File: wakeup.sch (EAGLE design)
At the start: 14 parts, among them IC2 ATMEGA48/88/168-AU

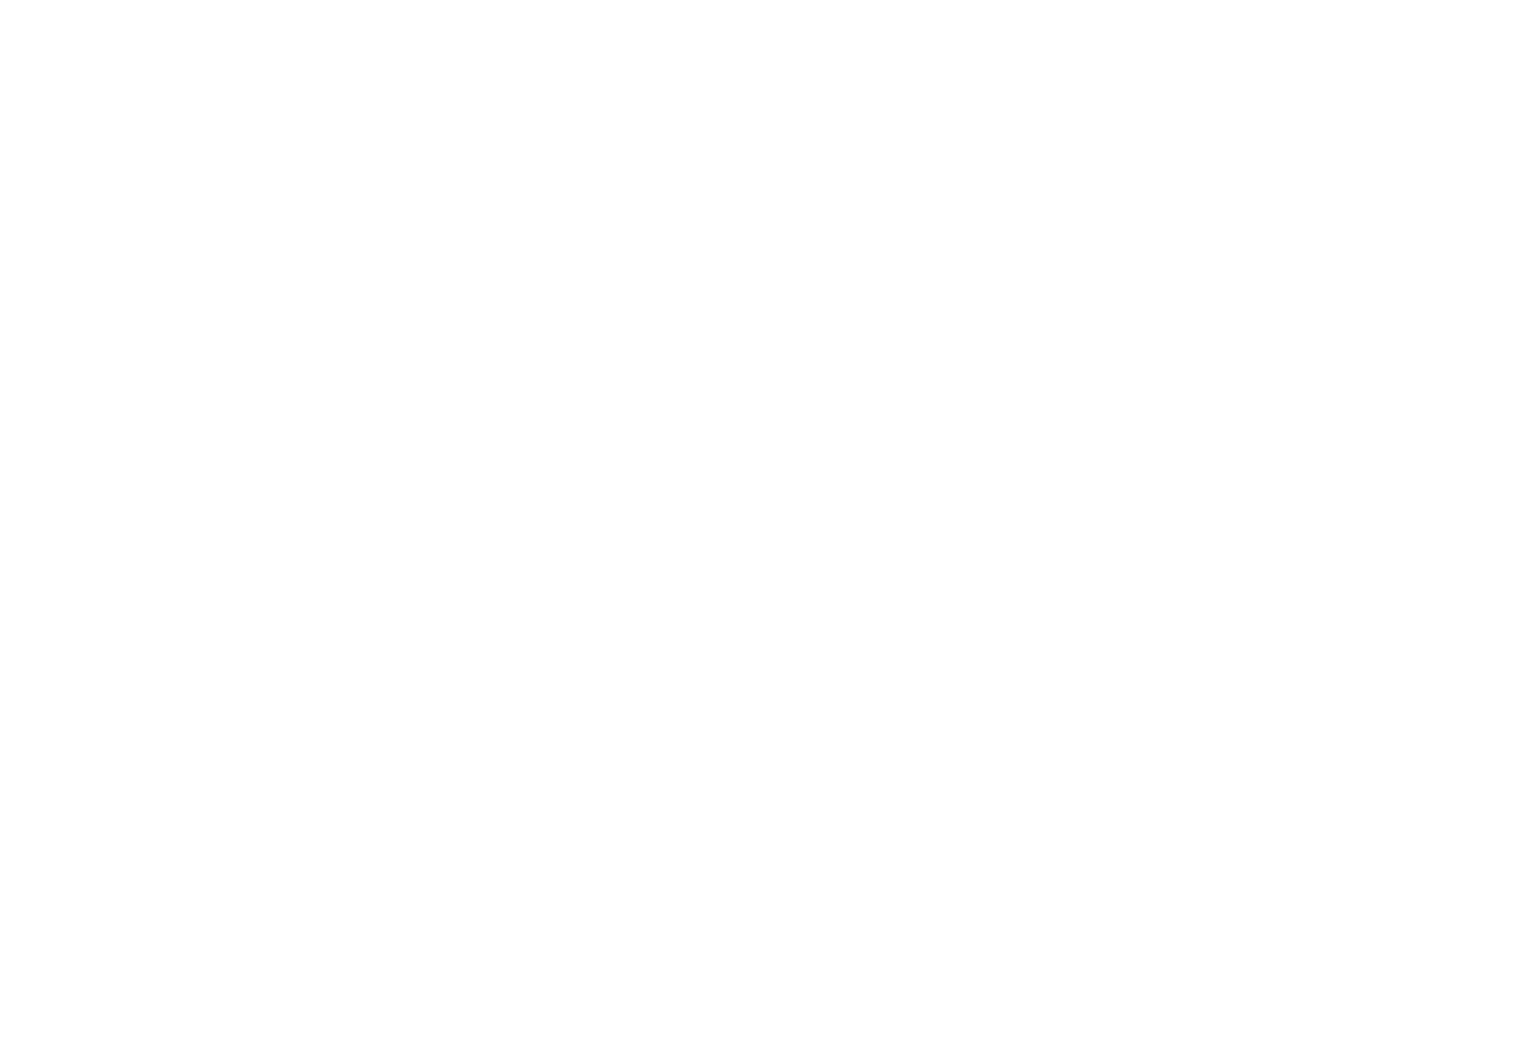
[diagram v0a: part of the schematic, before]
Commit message: Added RaspberryPi Library
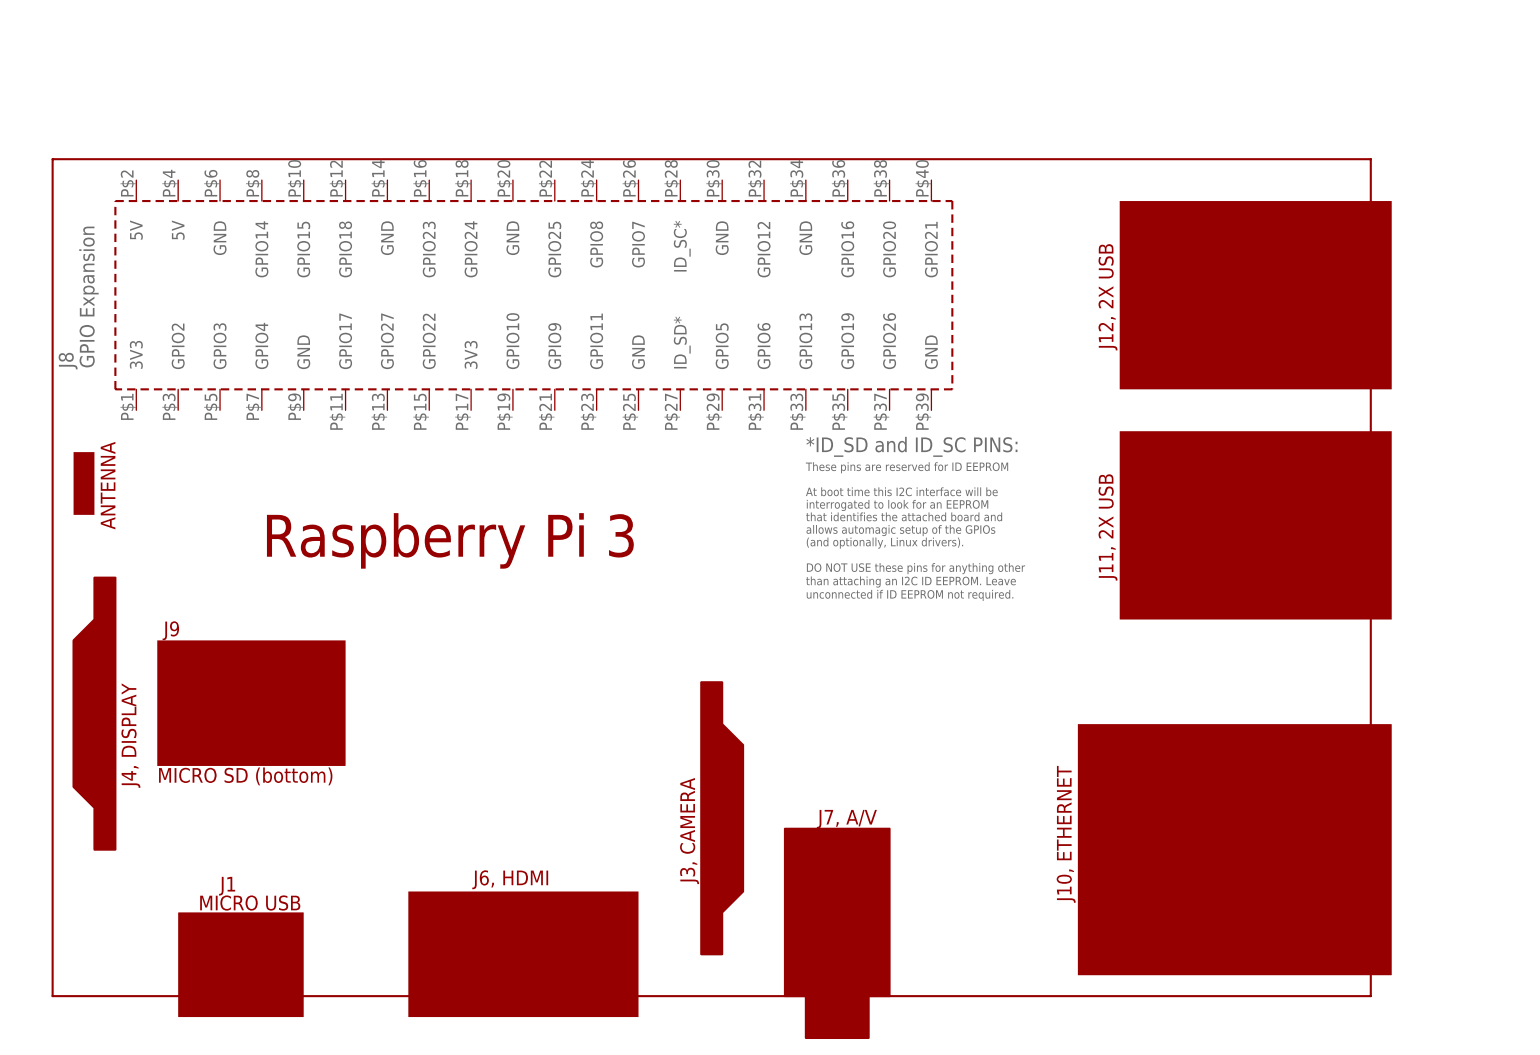
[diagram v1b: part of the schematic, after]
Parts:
- added PCB1: RPI3, e14_Rpi3_RevA:RPI3
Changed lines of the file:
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@@
 <?xml version="1.0" encoding="utf-8"?>
 <!DOCTYPE eagle SYSTEM "eagle.dtd">
-<eagle version="6.2">
+<eagle version="7.7.0">
 <drawing>
 <settings>
@@
 <layers>
 <layer number="1" name="Top" color="4" fill="1" visible="no" active="no"/>
+<layer number="2" name="Route2" color="1" fill="3" visible="no" active="no"/>
+<layer number="3" name="Route3" color="4" fill="3" visible="no" active="no"/>
+<layer number="4" name="Route4" color="1" fill="4" visible="no" active="no"/>
+<layer number="5" name="Route5" color="4" fill="4" visible="no" active="no"/>
+<layer number="6" name="Route6" color="1" fill="8" visible="no" active="no"/>
+<layer number="7" name="Route7" color="4" fill="8" visible="no" active="no"/>
+<layer number="8" name="Route8" color="1" fill="2" visible="no" active="no"/>
+<layer number="9" name="Route9" color="4" fill="2" visible="no" active="no"/>
+<layer number="10" name="Route10" color="1" fill="7" visible="no" active="no"/>
+<layer number="11" name="Route11" color="4" fill="7" visible="no" active="no"/>
+<layer number="12" name="Route12" color="1" fill="5" visible="no" active="no"/>
+<layer number="13" name="Route13" color="4" fill="5" visible="no" active="no"/>
+<layer number="14" name="Route14" color="1" fill="6" visible="no" active="no"/>
+<layer number="15" name="Route15" color="4" fill="6" visible="no" active="no"/>
 <layer number="16" name="Bottom" color="1" fill="1" visible="no" active="no"/>
 <layer number="17" name="Pads" color="2" fill="1" visible="no" active="no"/>
@@
 <layer number="51" name="tDocu" color="7" fill="1" visible="no" active="no"/>
 <layer number="52" name="bDocu" color="7" fill="1" visible="no" active="no"/>
+<layer number="90" name="Modules" color="5" fill="1" visible="yes" active="yes"/>
 <layer number="91" name="Nets" color="2" fill="1" visible="yes" active="yes"/>
 <layer number="92" name="Busses" color="1" fill="1" visible="yes" active="yes"/>
@@
 <part name="P+4" library="supply1" deviceset="VCC" device=""/>
 <part name="GND12" library="supply1" deviceset="GND" device=""/>
+<part name="PCB1" library="e14_Rpi3_RevA" deviceset="RPI3" device=""/>
 </parts>
 <sheets>
@@
 <instance part="P+4" gate="VCC" x="-27.94" y="45.72"/>
 <instance part="GND12" gate="1" x="-27.94" y="-2.54"/>
+<instance part="PCB1" gate="G$1" x="-96.52" y="-193.04"/>
 </instances>
 <busses>
@@
 </schematic>
 </drawing>
+<compatibility>
+<note version="6.3" minversion="6.2.2" severity="warning">
+Since Version 6.2.2 text objects can contain more than one line,
+which will not be processed correctly with this version.
+</note>
+</compatibility>
 </eagle>

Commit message: Updated board and schematics for RaspberryPI
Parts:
- removed PCB1: RPI3, e14_Rpi3_RevA:RPI3
- added C1: 100nF, resistor:C-EUC0805K
- added CFG: (no value), FLYFISH:PIN2_100
- added K1: PIN20X2, FLYFISH:PIN20X2
- added R1, R2: 3k9, resistor:R-EU_M0805
- added R3: 1k, resistor:R-EU_M0805
- added U1: EEPROM24, FLYFISH:EEPROM24
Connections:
- new net +3V3: C1.1, K1.1, K1.17, R1.2, R2.2, R3.2, U1.VCC
- new net +5V: K1.2, K1.4
- new net N$1: K1.28, R1.1, U1.SCL
- new net N$2: K1.27, R2.1, U1.SDA
- new net N$3: CFG.1, R3.1, U1.WP
- net GND: now also C1.2, CFG.2, K1.14, K1.20, K1.25, K1.30, K1.34, K1.39, K1.6, K1.9, U1.A0, U1.A1, U1.A2, U1.GND
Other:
- note added: "Checked by:"
- note added: "Drawn by:"
- note added: "v0.1"
- moved on the sheet: C2, C3, IC2, SL1, SL2-1, SL2-2, SV1, U$1, U$2, U$3, U$4, U$5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

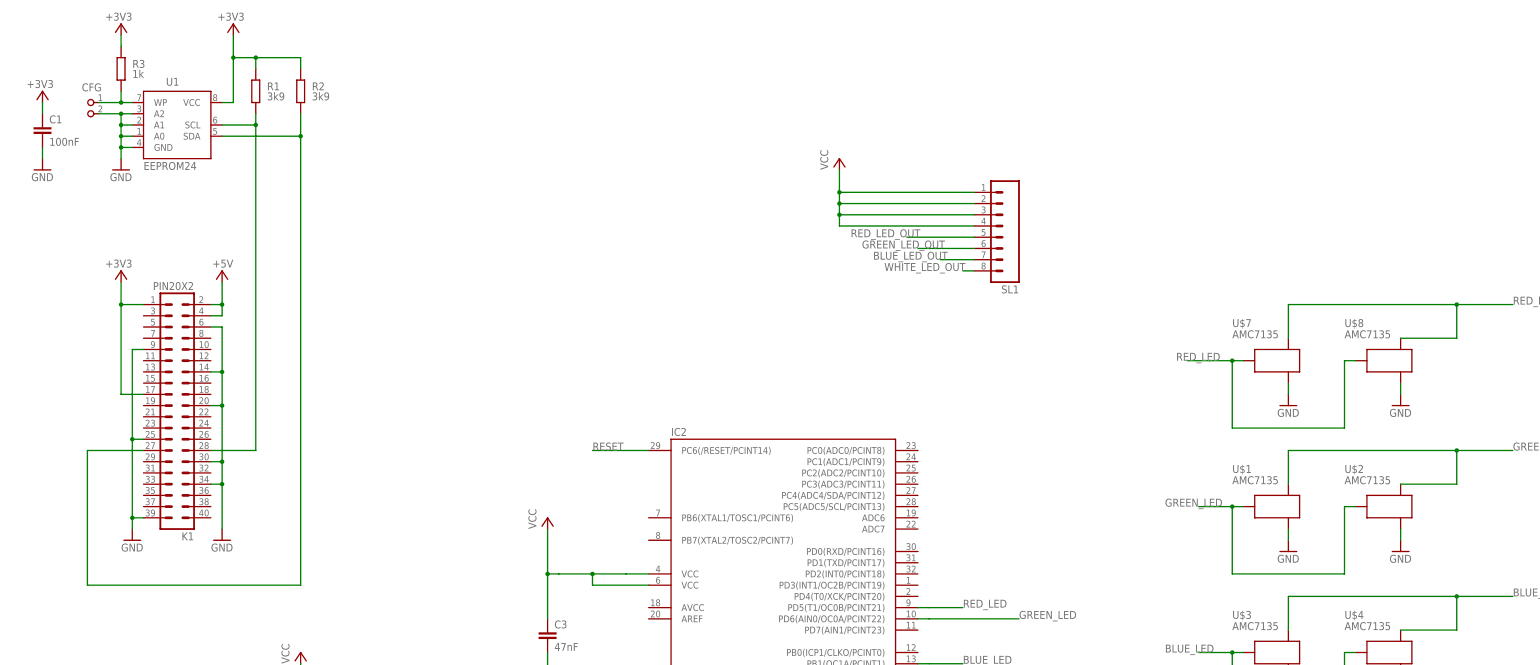
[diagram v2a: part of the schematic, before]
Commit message: Added Power connector and named some nets
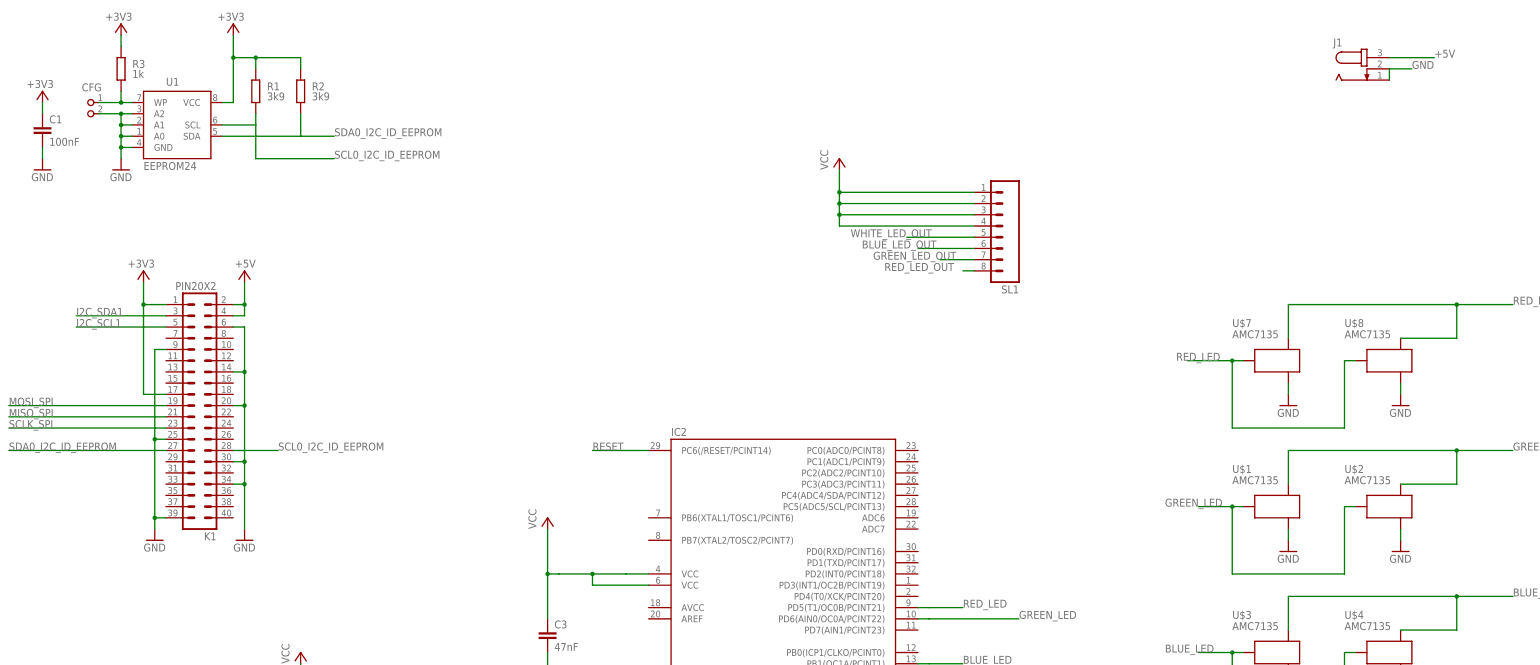
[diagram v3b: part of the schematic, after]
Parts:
- added J1: (no value), con-jack:JACK-PLUG1
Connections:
- net N$1 renamed SCL0_I2C_ID_EEPROM
- net N$2 renamed SDA0_I2C_ID_EEPROM
- new net I2C_SCL1: K1.5
- new net I2C_SDA1: K1.3
- new net MISO_SPI: K1.21
- new net MOSI_SPI: K1.19
- new net SCLK_SPI: K1.23
- net +5V: now also J1.3, SL1.1, SL1.2, SL1.3, SL1.4
- net BLUE_LED_OUT: now also SL1.6; no longer SL1.7
- net GND: now also J1.1, J1.2
- net GREEN_LED_OUT: now also SL1.7; no longer SL1.6
- net RED_LED_OUT: now also SL1.8; no longer SL1.5
- net VCC: no longer SL1.1, SL1.2, SL1.3, SL1.4
- net WHITE_LED_OUT: now also SL1.5; no longer SL1.8
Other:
- moved on the sheet: K1
